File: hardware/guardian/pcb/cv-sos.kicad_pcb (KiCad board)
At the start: 2 copper layers, 100.4 x 71 mm, 33 parts, among them J1 USB-C 16P, M1 SIM800L, M2 NEO-6M / L80, SW1 Tactile 6mm (guarded), U1 ESP32-WROOM-32E (4MB), U3 TP4056 + DW01/8205

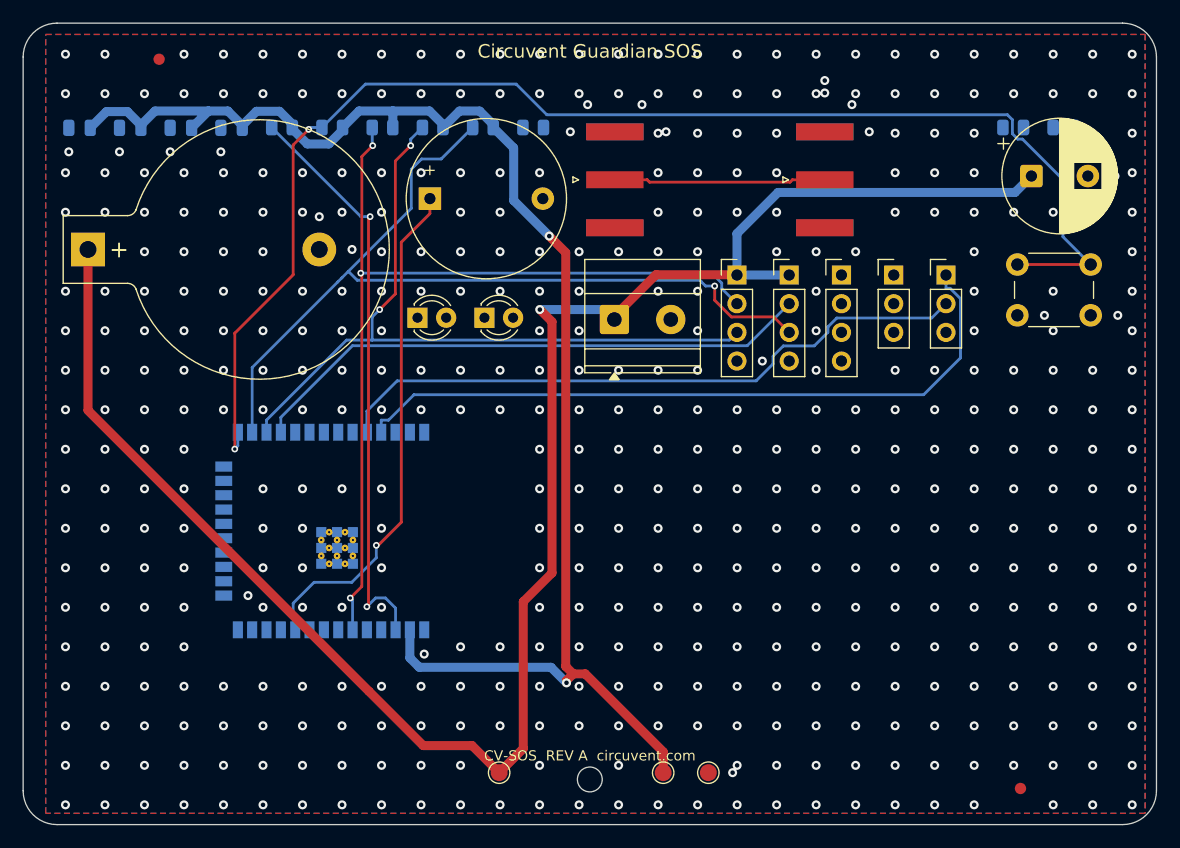
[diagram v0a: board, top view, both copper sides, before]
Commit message: hardware: fix mains isolation barrier gaps, add load-controller PCB
Adds the 13th board (ultra-compact dual-channel load controller: ESP32-C3,
opto+relay channel, MOSFET PWM channel, USB-C, AP2112K LDO, USBLC6 ESD) and
regenerates all 12 existing boards, which were stale with respect to earlier
relay-pinout and LED-polarity fixes.

The substantive change is to the mains isolation barrier. It is a keepout band
the router must not cross, deliberately cut where a component straddles it
because there the isolation is provided by the part's package. Three linked
defects made those cuts unsafe, each only visible once the previous was fixed:

1. The cut removed the barrier across the full band width for the straddling
   part's whole height, while the ISO_BRIDGE area that excuses the gap covered
   only the part itself. The router used the leftover strip beside the part to
   bring +5V within 6.99 mm of AC_N against an 8.0 mm reinforced creepage rule.
2. Straddling parts can overlap in y, so cutting per part put one part's
   keepout on another part's pads. The exempt x-ranges are now unioned per
   strip by a sweep line.
3. The rule only relaxes for items insideArea('ISO_BRIDGE'). With the hole the
   same size as the area, a track could hug the hole's edge without being
   contained in it, so the rule fired anyway and the router had no way to know.
   The hole is now the part's pad bbox + 0.3 mm, strictly inside ISO_BRIDGE at
   the footprint bbox + 0.6 mm.

The tighter hole leaves mains nets less room to reach bridge pads, so some
boards report more unconnected items. That is deliberate: those are documented
hand-routing items, whereas a creepage violation is a safety defect.

Also fixed in the generator:
- _pad_shape() derived a pad's layers from PAD::GetLayer(), which returns F.Cu
  even for pads on B.Cu. Every back-side pad became a phantom obstacle on the
  front, blocking legal paths there while hiding the real one behind. Only
  IsOnLayer() is truthful.
- Castella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
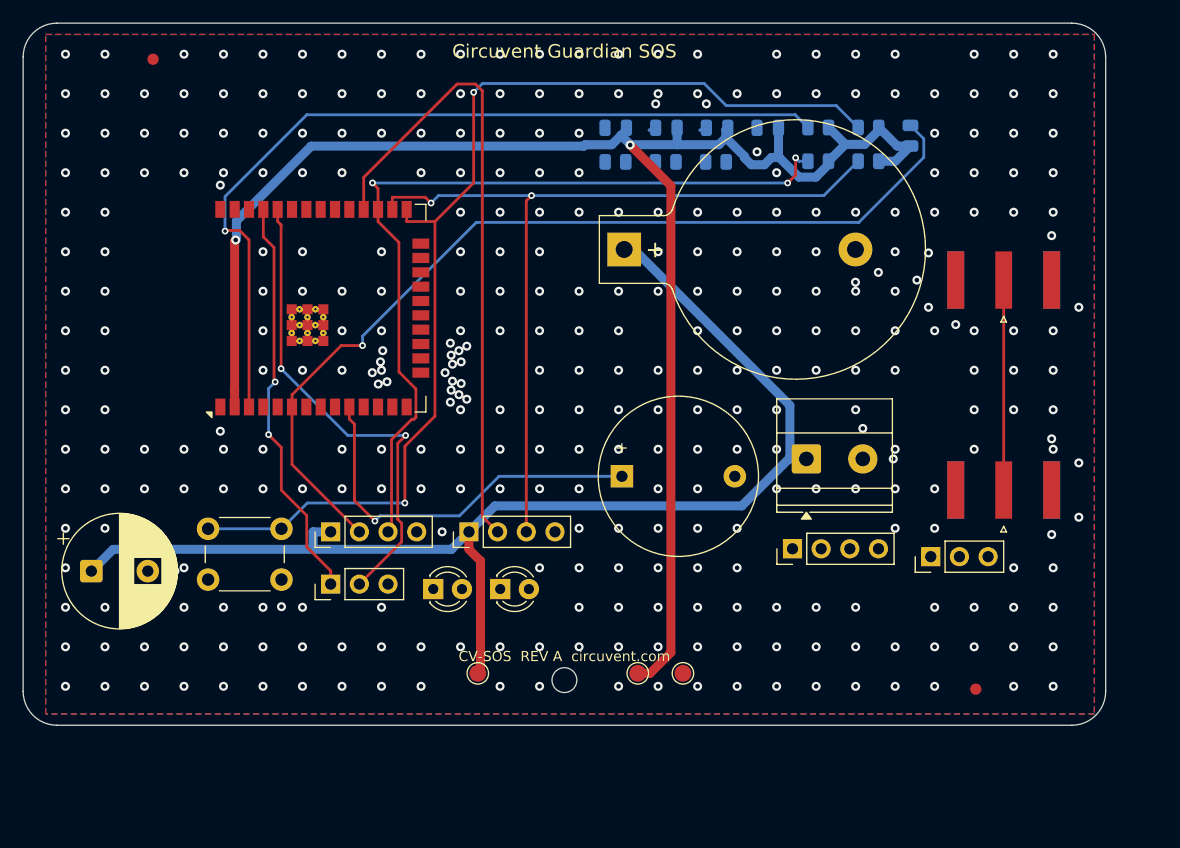
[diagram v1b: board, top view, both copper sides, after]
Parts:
- U1: moved to F.Cu
- moved C1 90.3 mm to (106.0, 128.5)
- moved SW1 75.4 mm to (116.4, 124.8)
- moved JP 61.0 mm to (127.2, 129.7), turned to 90 degrees
- moved C3 47.5 mm to (157.0, 89.3)
- moved BT1 47.5 mm to (153.2, 100.0)
- moved C2 47.5 mm to (152.5, 89.3)
- moved C4 47.5 mm to (161.5, 89.3)
- moved C5 47.5 mm to (166.0, 89.3)
- moved R1 47.5 mm to (170.4, 89.2)
- moved R2 47.5 mm to (174.9, 89.2)
- moved R3 46.8 mm to (178.6, 90.0), turned to 90 degrees
- moved M1 42.6 mm to (127.2, 125.1), turned to 90 degrees
- moved M2 36.4 mm to (139.5, 125.1), turned to 90 degrees
- moved ANT1 35.6 mm to (186.9, 102.8), turned to 90 degrees
- moved R4 34.3 mm to (170.4, 92.2)
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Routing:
- net +5V: track 163.5 -> 108.8 mm, vias 1 -> 0
- net UART_TX: track 62.8 -> 36.2 mm, vias 0 -> 2
- net EN: track 51.8 -> 75.5 mm, vias 2 -> 1
- net SOS_BTN: track 120.4 -> 96.9 mm
- net +3V3: track 129.6 -> 146.4 mm
- net UART_RX: track 57.8 -> 42.9 mm, vias 0 -> 2
- net BUZZER: track 45.3 -> 34.6 mm
- net SIM_RX: track 66.6 -> 74.1 mm, vias 2 -> 3
- net SIM_TX: track 50.5 -> 56.6 mm
- net GPS_RX: track 78.1 -> 74.1 mm, vias 1 -> 2
- net BATT_ADC: track 80.2 -> 83.1 mm, vias 3 -> 1
- net GND: track 0.00 -> 1.20 mm, vias 477 -> 360
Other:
- board size 100.4 x 71 mm -> 95.9 x 62.2 mm

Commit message: Release 1.10.0, and stop shipping permissions the app never uses
Cut 1.10.0 (versionCode 12) and built it: AAB 38 MB, APK 83 MB, signed with the
upload key, JS bundle embedded.

Checking the generated manifest before writing the Play listing turned up
permissions no one had asked for. Every one of them is printed on the store page
for users to read before they install:

  RECORD_AUDIO          expo-camera asks for the microphone so video can be
                        recorded with sound. This app only ever puts the camera
                        in barcode mode to read a QR label, and expo-speech is
                        output-only - it speaks, it does not listen. Left in,
                        Play lists "Microphone" against a home-control app,
                        which is alarming, unexplainable and untrue.
  SYSTEM_ALERT_WINDOW   React Native's development overlay, useless in a release
                        build and shown to users as "Display over other apps".
  READ/WRITE_EXTERNAL_STORAGE
                        Legacy storage access nothing here touches.

Stripped via android.blockedPermissions. That emits tools:node="remove", which
is a merge instruction rather than a guarantee, so it was checked against the
finished artifact with aapt2 rather than the source manifest - all four are
absent from the APK.

NEARBY_WIFI_DEVICES now carries neverForLocation. Android otherwise treats it as
location-capable, because knowing which networks are in range is enough to place
someone, and Play's data safety review treats it the same way. The app uses it
only to join a new device's setup hotspot. That flag is a promise, so the plugin
says plainly that it has to come off if scan results are ever used positionally.

What is left is defensible: location for Wi-Fi onboarding (Android requires it),
camera for the QR label, nearby-devices flagged as non-positional.

Added mobile/store/listing with the text Play asks for - title, short and full
descriptions, and what'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
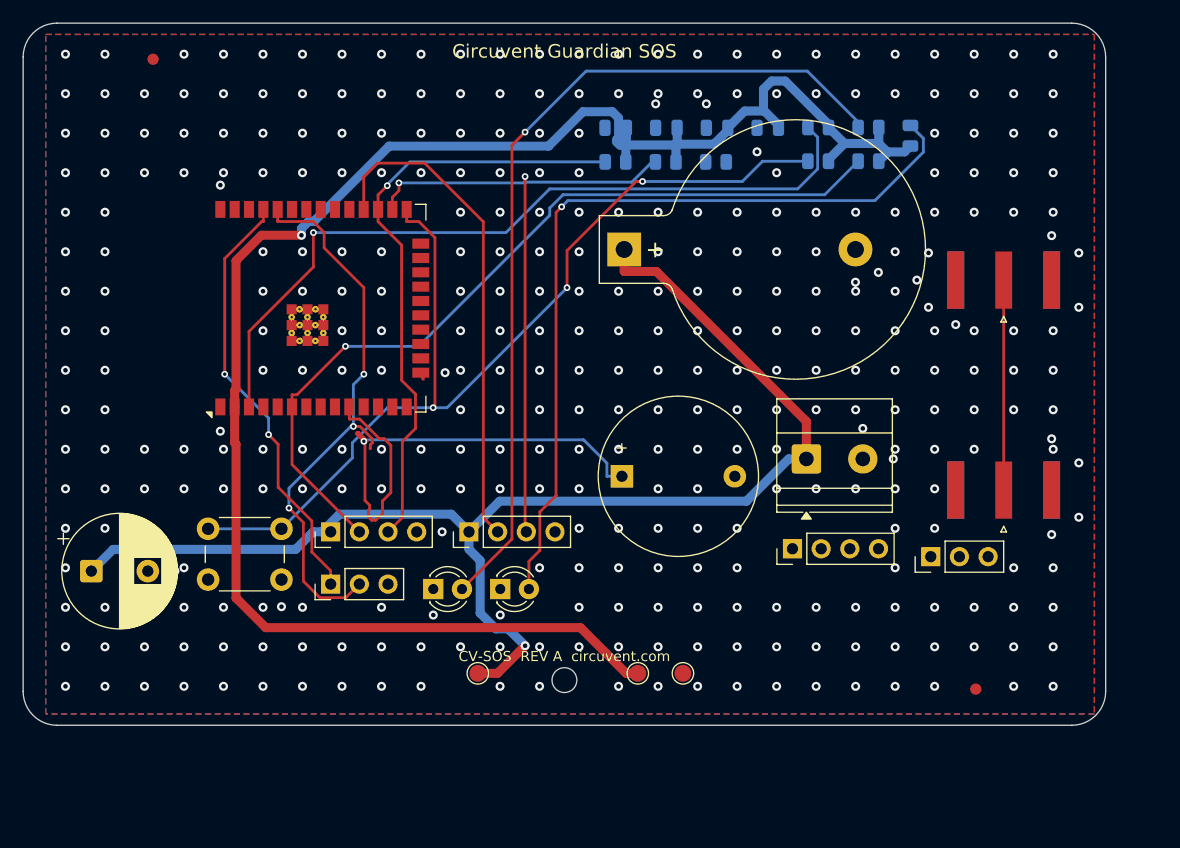
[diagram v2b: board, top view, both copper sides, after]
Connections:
- LED0 pad 1: N$LED0.1 -> GND
- LED0 pad 2: N$LED0.2 -> LED0_A
- LED1 pad 1: N$LED1.1 -> GND
- LED1 pad 2: N$LED1.2 -> LED1_A
- R2 pad 2: SOS_BTN -> LED0_A
- R3 pad 2: BATT_ADC -> LED1_A
- R4 pad 2: SIM_RX -> SOS_BTN
- R5 pad 2: GPS_RX -> BATT_ADC
- R6 pad 1: N$R6.1 -> +3V3
- R6 pad 2: N$R6.2 -> SIM_RX
- R7 pad 1: N$R7.1 -> +3V3
- R7 pad 2: N$R7.2 -> GPS_RX
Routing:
- net LED0_A: track 0.00 -> 76.9 mm, vias 0 -> 1
- net LED1_A: track 0.00 -> 72.0 mm, vias 0 -> 1
- net SIM_RX: track 74.1 -> 53.6 mm, vias 3 -> 1
- net GPS_RX: track 74.1 -> 58.1 mm
- net BUZZER: track 34.6 -> 47.9 mm
- net SIM_TX: track 56.6 -> 44.1 mm
- net +3V3: track 146.4 -> 155.9 mm, vias 2 -> 1
- net BATT_ADC: track 83.1 -> 73.7 mm
- net SOS_BTN: track 96.9 -> 88.6 mm, vias 2 -> 3
- net UART_RX: track 42.9 -> 50.5 mm, vias 2 -> 3
- net EN: track 75.5 -> 68.8 mm
- net +5V: track 108.8 -> 114.4 mm, vias 0 -> 1
- net UART_TX: track 36.2 -> 38.6 mm
- net GND: track 1.20 -> 0.60 mm, vias 360 -> 362
